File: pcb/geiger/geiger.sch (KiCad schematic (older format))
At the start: 121 parts, among them J1 Conn_01x02, J2 Conn_01x02, J3 Conn_01x03, J4 Conn_01x06, J5 Conn_01x02, J6 Conn_02x05_Odd_Even, J7 Conn_02x05_Odd_Even, K1 RELAY_DPST, Q1 BC140, Q2 BC107, Q3 BC211, Q4 AOT8N50, Q5 BC313, Q6 IRF540N, Q7 BC307, Q8 BC847, Q9 BC847, T1 Transformer_1P_1S, U1 MSP430G2553_PW20, U2 74HC595, U3 AD558, U4 MAA725, U5 LM2596, U6 MCP1402, X1 5.7MHz

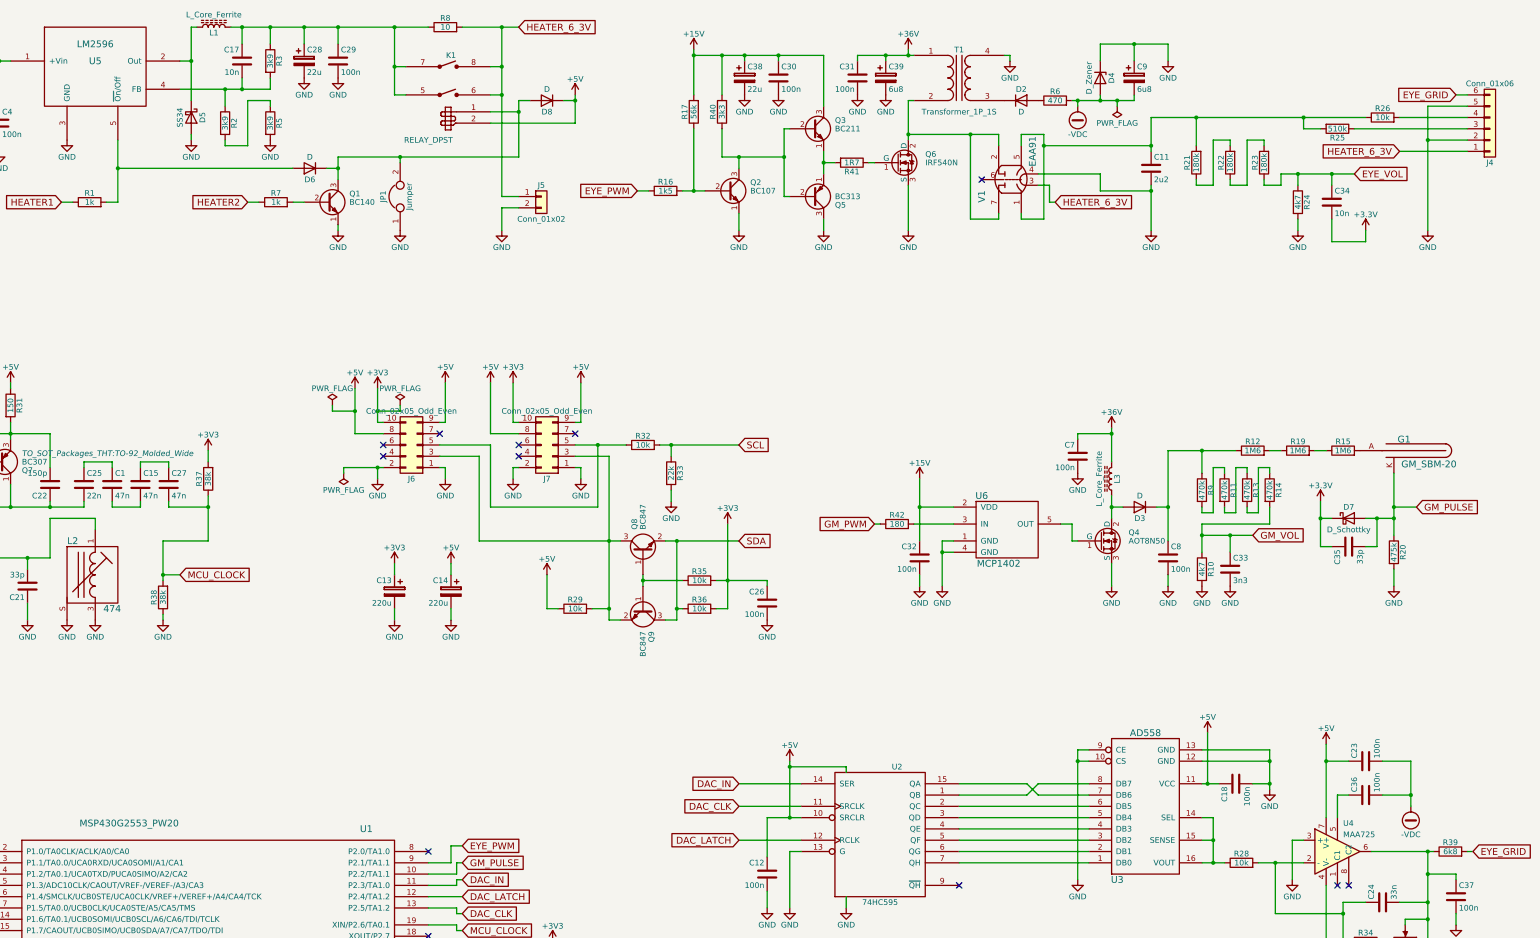
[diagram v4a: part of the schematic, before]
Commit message: Update geiger element values.
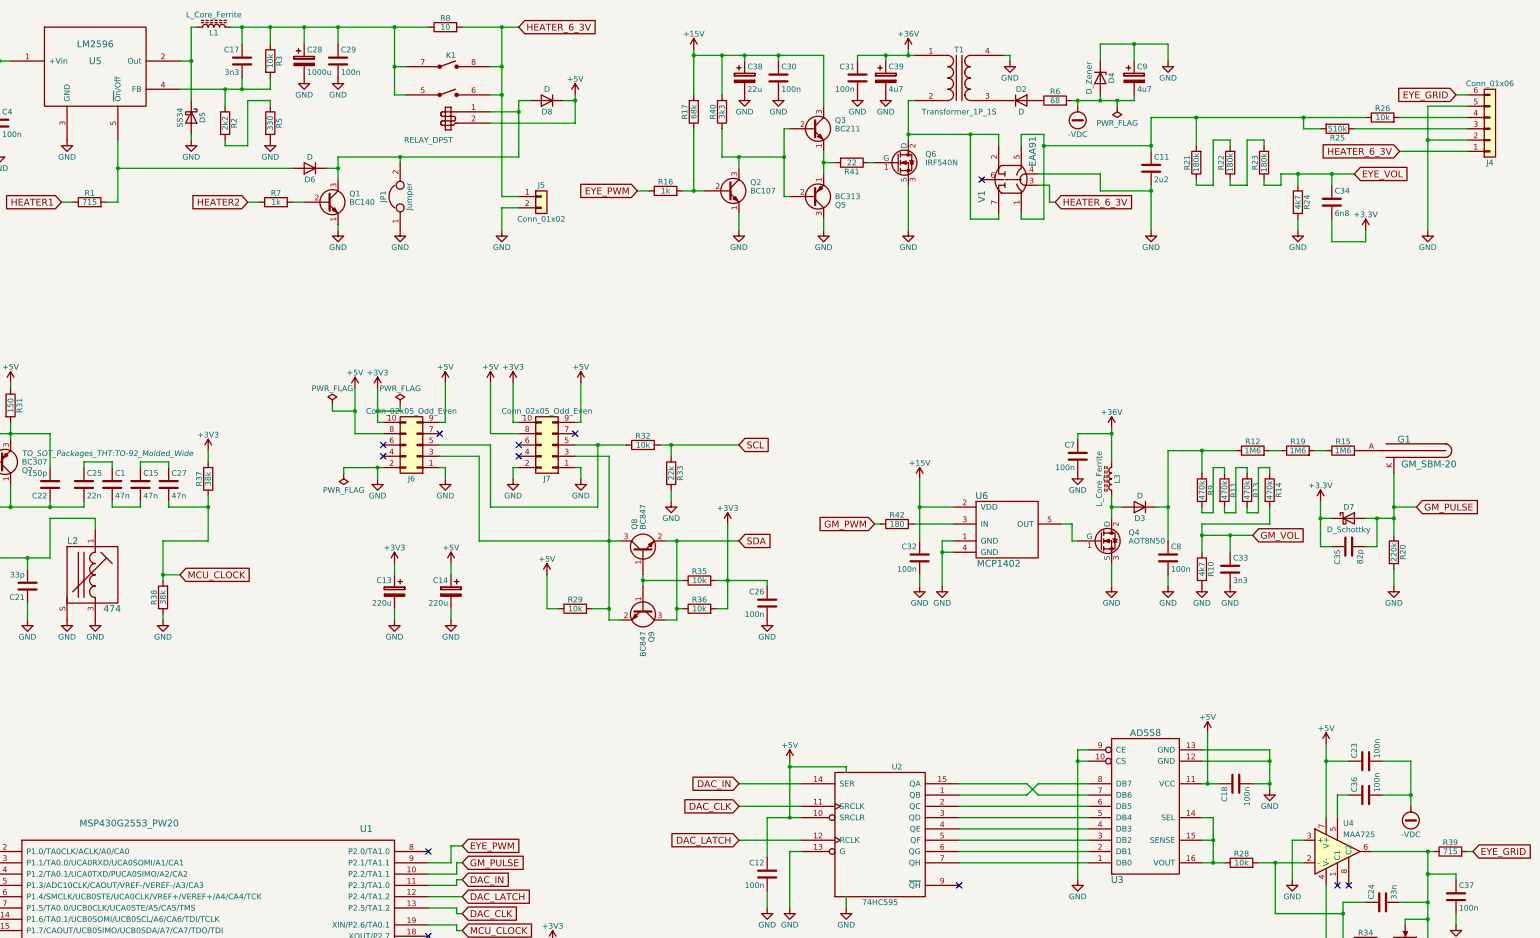
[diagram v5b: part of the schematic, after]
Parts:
- C17: value 10n -> 3n3
- C28: value 22u -> 1000u; footprint Capacitors_Tantalum_SMD:CP_Tantalum_Case-B_EIA-3528-21_Hand -> Capacitors_ThroughHole:CP_Radial_D8.0mm_P3.50mm
- C34: value 10n -> 6n8
- C35: value 33p -> 82p
- C39, C9: value 6u8 -> 4u7
- R1: value 1k -> 715
- R16: value 1k5 -> 1k
- R17: value 56k -> 68k
- R2: value 3k9 -> 2k2
- R20: value 475k -> 220k
- R3: value 3k9 -> 10k
- R39: value 6k8 -> 715
- R41: value 1R7 -> 22
- R5: value 3k9 -> 330
- R6: value 470 -> 68
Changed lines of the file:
@@
 P 11700 1750
 F 0 "R6" V 11780 1750 50  0000 C CNN
-F 1 "470" V 11700 1750 50  0000 C CNN
+F 1 "68" V 11700 1750 50  0000 C CNN
 F 2 "Resistors_ThroughHole:R_Axial_DIN0309_L9.0mm_D3.2mm_P12.70mm_Horizontal" V 11630 1750 50  0001 C CNN
 F 3 "" H 11700 1750 50  0001 C CNN
@@
 P 12400 1550
 F 0 "C9" H 12425 1650 50  0000 L CNN
-F 1 "6u8" H 12425 1450 50  0000 L CNN
+F 1 "4u7" H 12425 1450 50  0000 L CNN
 F 2 "Capacitors_Tantalum_SMD:CP_Tantalum_Case-D_EIA-7343-31_Hand" H 12438 1400 50  0001 C CNN
 F 3 "" H 12400 1550 50  0001 C CNN
@@
 P 14700 5750
 F 0 "R20" V 14780 5750 50  0000 C CNN
-F 1 "475k" V 14700 5750 50  0000 C CNN
+F 1 "220k" V 14700 5750 50  0000 C CNN
 F 2 "Resistors_SMD:R_1206_HandSoldering" V 14630 5750 50  0001 C CNN
 F 3 "" H 14700 5750 50  0001 C CNN
@@
 P 15200 8400
 F 0 "R39" V 15280 8400 50  0000 C CNN
-F 1 "6k8" V 15200 8400 50  0000 C CNN
+F 1 "715" V 15200 8400 50  0000 C CNN
 F 2 "Resistors_ThroughHole:R_Axial_DIN0309_L9.0mm_D3.2mm_P12.70mm_Horizontal" V 15130 8400 50  0001 C CNN
 F 3 "" H 15200 8400 50  0001 C CNN
@@
 P 4350 1950
 F 0 "R2" V 4430 1950 50  0000 C CNN
-F 1 "3k9" V 4350 1950 50  0000 C CNN
+F 1 "2k2" V 4350 1950 50  0000 C CNN
 F 2 "Resistors_SMD:R_1206_HandSoldering" V 4280 1950 50  0001 C CNN
 F 3 "" H 4350 1950 50  0001 C CNN
@@
 P 4750 1400
 F 0 "R3" V 4830 1400 50  0000 C CNN
-F 1 "3k9" V 4750 1400 50  0000 C CNN
+F 1 "10k" V 4750 1400 50  0000 C CNN
 F 2 "Resistors_SMD:R_1206_HandSoldering" V 4680 1400 50  0001 C CNN
 F 3 "" H 4750 1400 50  0001 C CNN
@@
 P 4500 1400
 F 0 "C17" H 4525 1500 50  0000 L CNN
-F 1 "10n" H 4525 1300 50  0000 L CNN
+F 1 "3n3" H 4525 1300 50  0000 L CNN
 F 2 "Capacitors_SMD:C_1206_HandSoldering" H 4538 1250 50  0001 C CNN
 F 3 "" H 4500 1400 50  0000 C CNN
@@
 P 5050 1400
 F 0 "C28" H 5075 1500 50  0000 L CNN
-F 1 "22u" H 5075 1300 50  0000 L CNN
-F 2 "Capacitors_Tantalum_SMD:CP_Tantalum_Case-B_EIA-3528-21_Hand" H 5088 1250 50  0001 C CNN
+F 1 "1000u" H 5075 1300 50  0000 L CNN
+F 2 "Capacitors_ThroughHole:CP_Radial_D8.0mm_P3.50mm" H 5088 1250 50  0001 C CNN
 F 3 "" H 5050 1400 50  0001 C CNN
 	1    5050 1400
@@
 P 3150 2650
 F 0 "R1" V 3230 2650 50  0000 C CNN
-F 1 "1k" V 3150 2650 50  0000 C CNN
+F 1 "715" V 3150 2650 50  0000 C CNN
 F 2 "Resistors_ThroughHole:R_Axial_DIN0411_L9.9mm_D3.6mm_P12.70mm_Horizontal" V 3080 2650 50  0001 C CNN
 F 3 "" H 3150 2650 50  0001 C CNN
@@
 P 4750 1950
 F 0 "R5" V 4830 1950 50  0000 C CNN
-F 1 "3k9" V 4750 1950 50  0000 C CNN
+F 1 "330" V 4750 1950 50  0000 C CNN
 F 2 "Resistors_SMD:R_1206_HandSoldering" V 4680 1950 50  0001 C CNN
 F 3 "" H 4750 1950 50  0001 C CNN
@@
 P 14300 5700
 F 0 "C35" H 14325 5800 50  0000 L CNN
-F 1 "33p" H 14325 5600 50  0000 L CNN
+F 1 "82p" H 14325 5600 50  0000 L CNN
 F 2 "Capacitors_ThroughHole:C_Rect_L9.0mm_W3.2mm_P7.50mm_MKT" H 14338 5550 50  0001 C CNN
 F 3 "" H 14300 5700 50  0000 C CNN
@@
 P 14150 2650
 F 0 "C34" H 14175 2750 50  0000 L CNN
-F 1 "10n" H 14175 2550 50  0000 L CNN
+F 1 "6n8" H 14175 2550 50  0000 L CNN
 F 2 "Capacitors_ThroughHole:C_Rect_L9.0mm_W3.2mm_P7.50mm_MKT" H 14188 2500 50  0001 C CNN
 F 3 "" H 14150 2650 50  0000 C CNN
@@
 P 9900 2300
 F 0 "R41" V 9980 2300 50  0000 C CNN
-F 1 "1R7" V 9900 2300 50  0000 C CNN
+F 1 "22" V 9900 2300 50  0000 C CNN
 F 2 "Resistors_ThroughHole:R_Axial_DIN0309_L9.0mm_D3.2mm_P12.70mm_Horizontal" V 9830 2300 50  0001 C CNN
 F 3 "" H 9900 2300 50  0001 C CNN
@@
 P 8500 1850
 F 0 "R17" V 8580 1850 50  0000 C CNN
-F 1 "56k" V 8500 1850 50  0000 C CNN
+F 1 "68k" V 8500 1850 50  0000 C CNN
 F 2 "Resistors_ThroughHole:R_Axial_DIN0207_L6.3mm_D2.5mm_P10.16mm_Horizontal" V 8430 1850 50  0001 C CNN
 F 3 "" H 8500 1850 50  0001 C CNN
@@
 P 8250 2550
 F 0 "R16" V 8330 2550 50  0000 C CNN
-F 1 "1k5" V 8250 2550 50  0000 C CNN
+F 1 "1k" V 8250 2550 50  0000 C CNN
 F 2 "Resistors_ThroughHole:R_Axial_DIN0207_L6.3mm_D2.5mm_P10.16mm_Horizontal" V 8180 2550 50  0001 C CNN
 F 3 "" H 8250 2550 50  0001 C CNN
@@
 	7050 1750 6950 1750
 Wire Wire Line
-	6950 2250 6950 1750
+	6950 1750 6950 2250
 Wire Wire Line
 	6950 1850 6700 1850
 Wire Wire Line
-	5350 2250 6950 2250
+	6950 2250 5350 2250
 Connection ~ 6950 1850
 Connection ~ 5900 2250
@@
 P 10200 1550
 F 0 "C39" H 10225 1650 50  0000 L CNN
-F 1 "6u8" H 10225 1450 50  0000 L CNN
+F 1 "4u7" H 10225 1450 50  0000 L CNN
 F 2 "Capacitors_Tantalum_SMD:CP_Tantalum_Case-D_EIA-7343-31_Hand" H 10238 1400 50  0001 C CNN
 F 3 "" H 10200 1550 50  0001 C CNN

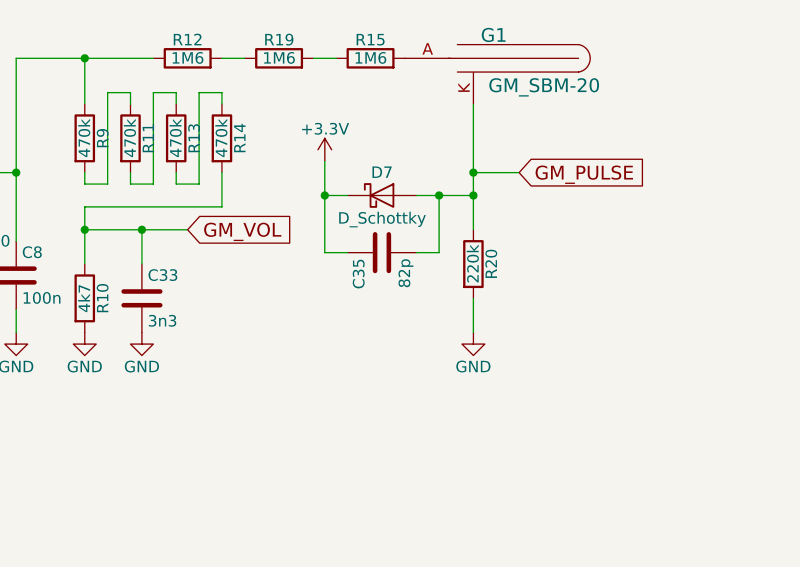
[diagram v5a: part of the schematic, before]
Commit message: Update element values on geiger board.
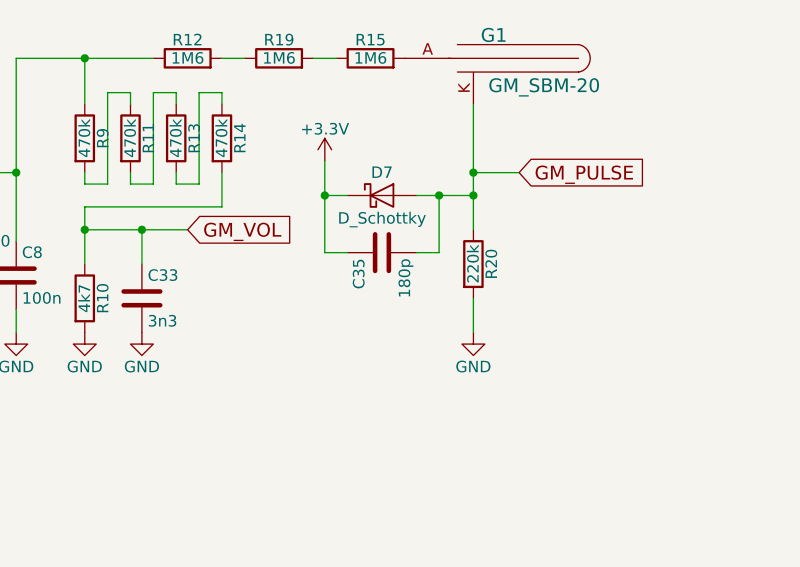
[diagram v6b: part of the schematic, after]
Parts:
- C35: value 82p -> 180p
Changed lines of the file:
@@
 P 14300 5700
 F 0 "C35" H 14325 5800 50  0000 L CNN
-F 1 "82p" H 14325 5600 50  0000 L CNN
+F 1 "180p" H 14325 5600 50  0000 L CNN
 F 2 "Capacitors_ThroughHole:C_Rect_L9.0mm_W3.2mm_P7.50mm_MKT" H 14338 5550 50  0001 C CNN
 F 3 "" H 14300 5700 50  0000 C CNN

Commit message: Update all Kicad files to Kicad 5.
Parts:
- C1, C10, C11, C12, C15, C16, C17, C18, C19, C20, C21, C22, C23, C24, C25, C26, C27, C29, C3, C30, C31, C32, C33, C34, C35, C36, C37, C4, C7, C8: symbol C -> geiger-rescue:C
- C13, C14, C2, C28, C38, C39, C5, C6, C9: symbol CP -> geiger-rescue:CP
- D1, D4: symbol D_Zener -> geiger-rescue:D_Zener
- D2, D3, D6, D8: symbol D -> geiger-rescue:D
- D5, D7: symbol D_Schottky -> geiger-rescue:D_Schottky
- G1: symbol GM_SBM-20 -> geiger-rescue:GM_SBM-20
- J1, J2, J5: symbol Conn_01x02 -> geiger-rescue:Conn_01x02
- J3: symbol Conn_01x03 -> geiger-rescue:Conn_01x03
- J4: symbol Conn_01x06 -> geiger-rescue:Conn_01x06
- J6, J7: symbol Conn_02x05_Odd_Even -> geiger-rescue:Conn_02x05_Odd_Even
- JP1: symbol Jumper -> geiger-rescue:Jumper
- K1: symbol RELAY_DPST -> geiger-rescue:RELAY_DPST
- L1, L3: symbol L_Core_Ferrite -> geiger-rescue:L_Core_Ferrite
- L2: symbol L_7x7 -> geiger-rescue:L_7x7
- Q1, Q3: symbol BC140 -> geiger-rescue:BC140
- Q2: symbol BC107 -> geiger-rescue:BC107
- Q4, Q6: symbol IRF540N -> geiger-rescue:IRF540N
- Q5: symbol BC160 -> geiger-rescue:BC160
- Q7: symbol BC307 -> geiger-rescue:BC307
- Q8, Q9: symbol BC847 -> geiger-rescue:BC847
- R1, R10, R11, R12, R13, R14, R15, R16, R17, R18, R19, R2, R20, R21, R22, R23, R24, R25, R26, R27, R28, R29, R3, R30, R31, R32, R33, R34, R36, R37, R38, R39, R4, R40, R41, R42, R5, R6, R7, R8, R9: symbol R -> geiger-rescue:R
- R35: value 10k -> 4k7; symbol R -> geiger-rescue:R
- RV1: symbol POT -> geiger-rescue:POT
- T1: symbol Transformer_1P_1S -> geiger-rescue:Transformer_1P_1S
- U1: symbol MSP430G2553_PW20 -> geiger-rescue:MSP430G2553_PW20
- U2: symbol 74HC595 -> geiger-rescue:74HC595
- U3: symbol AD558 -> geiger-rescue:AD558
- U4: symbol MAA725 -> geiger-rescue:MAA725
- U5: symbol LM2596 -> geiger-rescue:LM2596
- U6: symbol MCP1402 -> geiger-rescue:MCP1402
- V1: symbol EAA91 -> geiger-rescue:EAA91
- X1: symbol CRYSTAL_SMD -> geiger-rescue:CRYSTAL_SMD

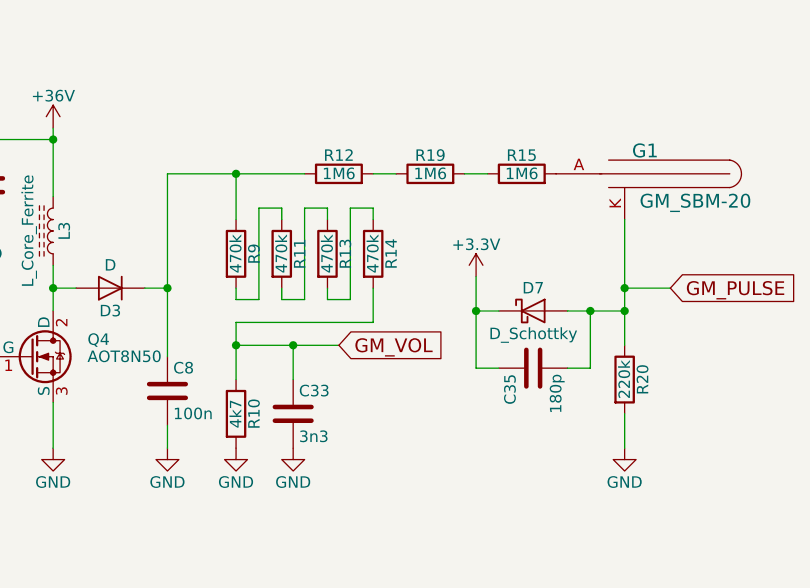
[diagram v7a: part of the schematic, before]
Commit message: Update values on PCB.
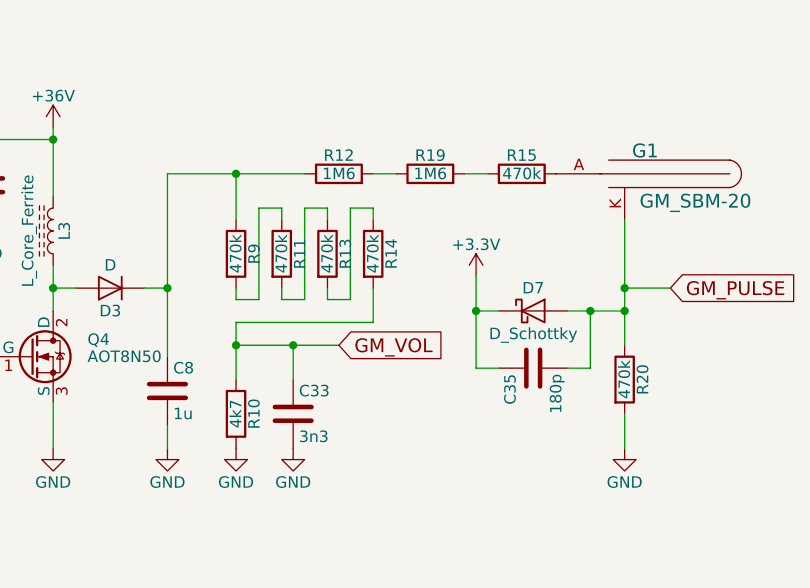
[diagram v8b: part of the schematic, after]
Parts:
- C8: value 100n -> 1u
- R15: value 1M6 -> 470k
- R20: value 220k -> 470k
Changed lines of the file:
@@
 P 12700 5800
 F 0 "C8" H 12725 5900 50  0000 L CNN
-F 1 "100n" H 12725 5700 50  0000 L CNN
+F 1 "1u" H 12725 5700 50  0000 L CNN
 F 2 "Capacitors_ThroughHole:C_Rect_L33.0mm_W13.0mm_P27.50mm_MKS4" H 12738 5650 50  0001 C CNN
 F 3 "" H 12700 5800 50  0000 C CNN
@@
 P 14250 4850
 F 0 "R15" V 14330 4850 50  0000 C CNN
-F 1 "1M6" V 14250 4850 50  0000 C CNN
+F 1 "470k" V 14250 4850 50  0000 C CNN
 F 2 "Resistors_ThroughHole:R_Axial_DIN0309_L9.0mm_D3.2mm_P12.70mm_Horizontal" V 14180 4850 50  0001 C CNN
 F 3 "" H 14250 4850 50  0001 C CNN
@@
 P 14700 5750
 F 0 "R20" V 14780 5750 50  0000 C CNN
-F 1 "220k" V 14700 5750 50  0000 C CNN
+F 1 "470k" V 14700 5750 50  0000 C CNN
 F 2 "Resistors_SMD:R_1206_HandSoldering" V 14630 5750 50  0001 C CNN
 F 3 "" H 14700 5750 50  0001 C CNN
